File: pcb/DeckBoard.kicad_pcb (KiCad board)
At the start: 2 copper layers, 212 x 67 mm, 75 parts, among them J1 Thumbstick Connector, SW1 SW_Push, SW10 SW_Push, SW11 SW_Push, SW12 SW_Push, SW13 SW_Push, SW14 SW_Push, SW15 SW_Push, SW16 SW_Push, SW17 SW_Push, SW18 SW_Push, SW19 SW_Push, SW2 SW_Push, SW20 SW_Push, SW21 SW_Push, SW22 SW_Push, SW23 SW_Push, SW24 SW_Push, SW25 SW_Push, SW26 SW_Push, SW27 SW_Push, SW28 SW_Push, SW29 SW_Push, SW3 SW_Push, SW30 SW_Push, SW31 SW_Push, SW32 SW_Push, SW33 SW_Push, SW34 SW_Push, SW35 SW_Push, SW36 SW_Push, SW4 SW_Push, SW5 SW_Push, SW6 SW_Push, SW7 SW_Push, SW8 SW_Push, SW9 SW_Push, U1 ProMicro

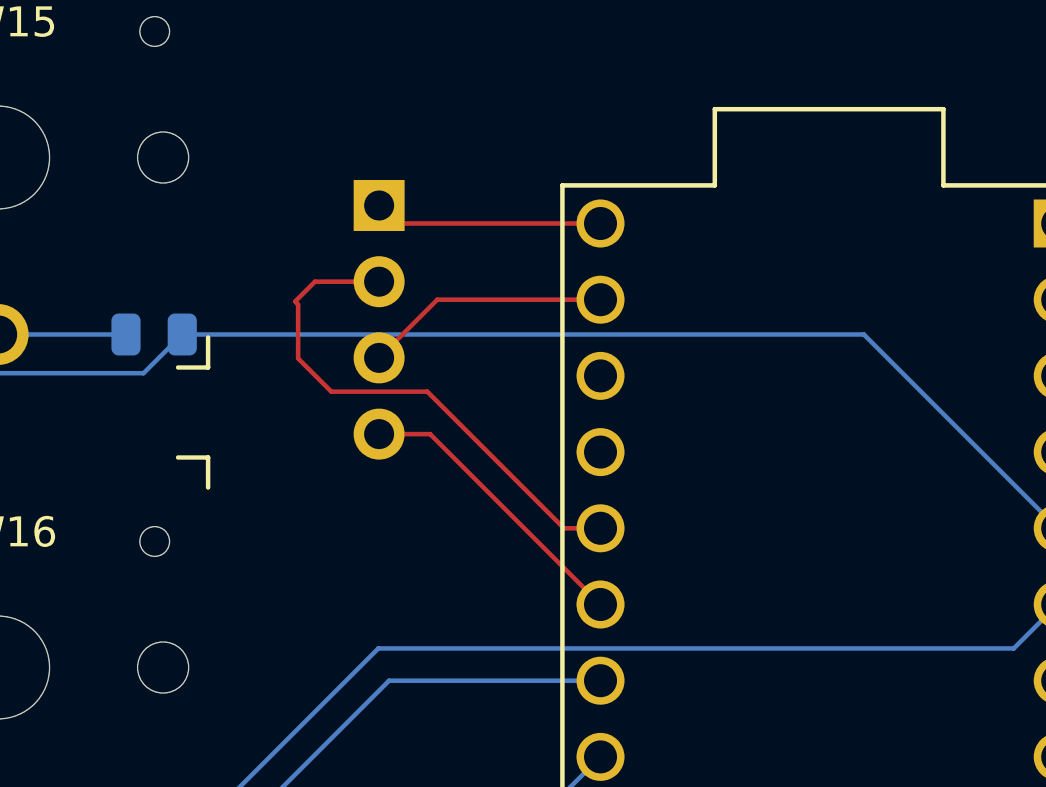
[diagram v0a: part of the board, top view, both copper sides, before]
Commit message: Fixed trace intersecting pad and moved joystick closer
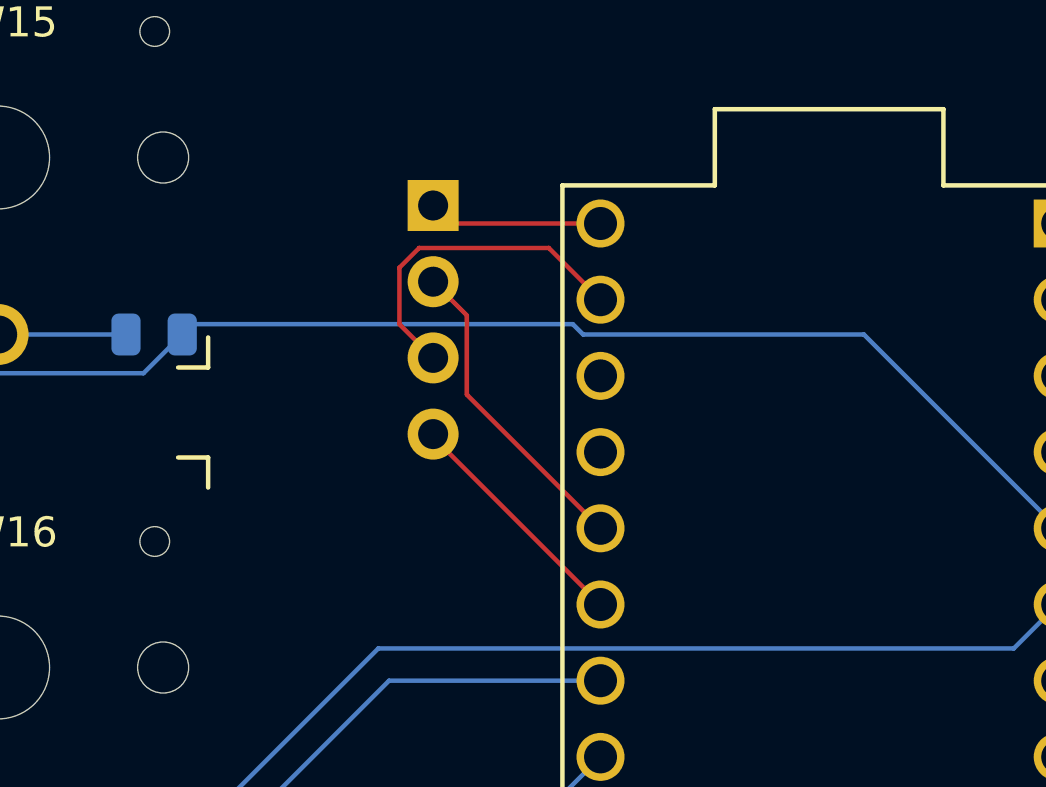
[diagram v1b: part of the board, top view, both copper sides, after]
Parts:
- moved J1 1.80 mm to (113.5, 38.6)
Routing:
- net Net-(J1-Pin_2): track 17.4 -> 10.5 mm
- net Net-(J1-Pin_3): track 8.18 -> 11.2 mm
- net Net-(J1-Pin_1): track 7.63 -> 5.83 mm
- net Net-(J1-Pin_4): track 9.73 -> 7.99 mm
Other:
- board text added: "cyberdeck keyboard v1.1 ilthraim 2023 inspired by u/brickbots cyberdeck"
- board text removed: "cyberdeck keyboard ilthraim 2023 inspired by u/brickbots cyberdeck"
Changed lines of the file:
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@@
   )
   (footprint "Connector_PinHeader_2.54mm:PinHeader_1x04_P2.54mm_Vertical" (layer "B.Cu")
-    (at 111.7 38.6 180)
+    (at 113.5 38.6 180)
     (descr "Through hole straight pin header, 1x04, 2.54mm pitch, single row")
     (tags "Through hole pin header THT 1x04 2.54mm single row")
@@
   (gr_line (start 179 96) (end 232 80)
     (stroke (width 0.1) (type default)) (layer "Edge.Cuts"))
-  (gr_text "cyberdeck keyboard\nilthraim 2023\ninspired by u/brickbots cyberdeck" (at 210.2 85) (layer "B.SilkS")
+  (gr_text "cyberdeck keyboard v1.1\nilthraim 2023\ninspired by u/brickbots cyberdeck" (at 210.2 85) (layer "B.SilkS")
     (effects (font (size 1 1) (thickness 0.15)) (justify left bottom mirror))
   )
   (segment (start 97.17425 42.9) (end 98.46525 44.191) (width 0.15) (layer "B.Cu") (net 1))
   (segment (start 52.4285 44.191) (end 67.8465 44.191) (width 0.15) (layer "B.Cu") (net 1))
+  (segment (start 118.5 42.9) (end 127.86 42.9) (width 0.15) (layer "B.Cu") (net 1))
   (segment (start 85.8465 44.191) (end 87.1375 42.9) (width 0.15) (layer "B.Cu") (net 1))
   (segment (start 195.1375 42.9) (end 193.8465 44.191) (width 0.15) (layer "B.Cu") (net 1))
@@
   (segment (start 127.86 42.9) (end 134.32 49.36) (width 0.15) (layer "B.Cu") (net 1))
   (segment (start 70.4285 44.191) (end 85.8465 44.191) (width 0.15) (layer "B.Cu") (net 1))
+  (segment (start 105.4825 42.555) (end 118.155 42.555) (width 0.15) (layer "B.Cu") (net 1))
   (segment (start 103.8465 44.191) (end 105.1375 42.9) (width 0.15) (layer "B.Cu") (net 1))
   (segment (start 218.8625 42.9) (end 213.1375 42.9) (width 0.15) (layer "B.Cu") (net 1))
@@
   (segment (start 193.8465 44.191) (end 178.4285 44.191) (width 0.15) (layer "B.Cu") (net 1))
   (segment (start 51.1375 42.9) (end 52.4285 44.191) (width 0.15) (layer "B.Cu") (net 1))
-  (segment (start 105.1375 42.9) (end 127.86 42.9) (width 0.15) (layer "B.Cu") (net 1))
   (segment (start 98.46525 44.191) (end 103.8465 44.191) (width 0.15) (layer "B.Cu") (net 1))
   (segment (start 211.8465 44.191) (end 196.4285 44.191) (width 0.15) (layer "B.Cu") (net 1))
+  (segment (start 118.155 42.555) (end 118.5 42.9) (width 0.15) (layer "B.Cu") (net 1))
   (segment (start 166.1 42.9) (end 159.1375 42.9) (width 0.15) (layer "B.Cu") (net 1))
   (segment (start 49.8465 44.191) (end 51.1375 42.9) (width 0.15) (layer "B.Cu") (net 1))
@@
   (segment (start 43.17425 42.9) (end 44.46525 44.191) (width 0.15) (layer "B.Cu") (net 1))
   (segment (start 67.8465 44.191) (end 69.1375 42.9) (width 0.15) (layer "B.Cu") (net 1))
+  (segment (start 105.1375 42.9) (end 105.4825 42.555) (width 0.15) (layer "B.Cu") (net 1))
   (segment (start 87.1375 42.9) (end 97.17425 42.9) (width 0.15) (layer "B.Cu") (net 1))
   (segment (start 213.1375 42.9) (end 211.8465 44.191) (width 0.15) (layer "B.Cu") (net 1))
@@
   (segment (start 218.56316 74.8) (end 206.76316 63) (width 0.15) (layer "B.Cu") (net 50))
   (segment (start 206.76316 63) (end 145 63) (width 0.15) (layer "B.Cu") (net 50))
-  (segment (start 112.3 39.2) (end 111.7 38.6) (width 0.15) (layer "F.Cu") (net 55))
-  (segment (start 119.08 39.2) (end 112.3 39.2) (width 0.15) (layer "F.Cu") (net 55))
-  (segment (start 119.08 49.36) (end 117.86 49.36) (width 0.15) (layer "F.Cu") (net 56))
-  (segment (start 110.105 44.805) (end 109 43.7) (width 0.15) (layer "F.Cu") (net 56))
-  (segment (start 108.9 41.8) (end 109.56 41.14) (width 0.15) (layer "F.Cu") (net 56))
-  (segment (start 109 41.9) (end 108.9 41.8) (width 0.15) (layer "F.Cu") (net 56))
-  (segment (start 117.86 49.36) (end 113.305 44.805) (width 0.15) (layer "F.Cu") (net 56))
-  (segment (start 109.56 41.14) (end 111.7 41.14) (width 0.15) (layer "F.Cu") (net 56))
-  (segment (start 113.305 44.805) (end 110.105 44.805) (width 0.15) (layer "F.Cu") (net 56))
-  (segment (start 109 43.7) (end 109 41.9) (width 0.15) (layer "F.Cu") (net 56))
-  (segment (start 119.08 41.74) (end 113.64 41.74) (width 0.15) (layer "F.Cu") (net 59))
-  (segment (start 113.64 41.74) (end 111.7 43.68) (width 0.15) (layer "F.Cu") (net 59))
-  (segment (start 111.7 46.22) (end 113.4 46.22) (width 0.15) (layer "F.Cu") (net 60))
-  (segment (start 113.4 46.22) (end 119.08 51.9) (width 0.15) (layer "F.Cu") (net 60))
+  (segment (start 114.1 39.2) (end 113.5 38.6) (width 0.15) (layer "F.Cu") (net 55))
+  (segment (start 119.08 39.2) (end 114.1 39.2) (width 0.15) (layer "F.Cu") (net 55))
+  (segment (start 114.625 44.905) (end 114.625 42.265) (width 0.15) (layer "F.Cu") (net 56))
+  (segment (start 114.625 42.265) (end 113.5 41.14) (width 0.15) (layer "F.Cu") (net 56))
+  (segment (start 119.08 49.36) (end 114.625 44.905) (width 0.15) (layer "F.Cu") (net 56))
+  (segment (start 117.355 40.015) (end 113.034009 40.015) (width 0.15) (layer "F.Cu") (net 59))
+  (segment (start 119.08 41.74) (end 117.355 40.015) (width 0.15) (layer "F.Cu") (net 59))
+  (segment (start 113.034009 40.015) (end 112.375 40.674009) (width 0.15) (layer "F.Cu") (net 59))
+  (segment (start 112.375 42.555) (end 113.5 43.68) (width 0.15) (layer "F.Cu") (net 59))
+  (segment (start 112.375 40.674009) (end 112.375 42.555) (width 0.15) (layer "F.Cu") (net 59))
+  (segment (start 113.5 46.32) (end 113.5 46.22) (width 0.15) (layer "F.Cu") (net 60))
+  (segment (start 119.08 51.9) (end 113.5 46.32) (width 0.15) (layer "F.Cu") (net 60))
 )
